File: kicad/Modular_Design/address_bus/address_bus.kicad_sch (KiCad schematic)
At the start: 21 parts

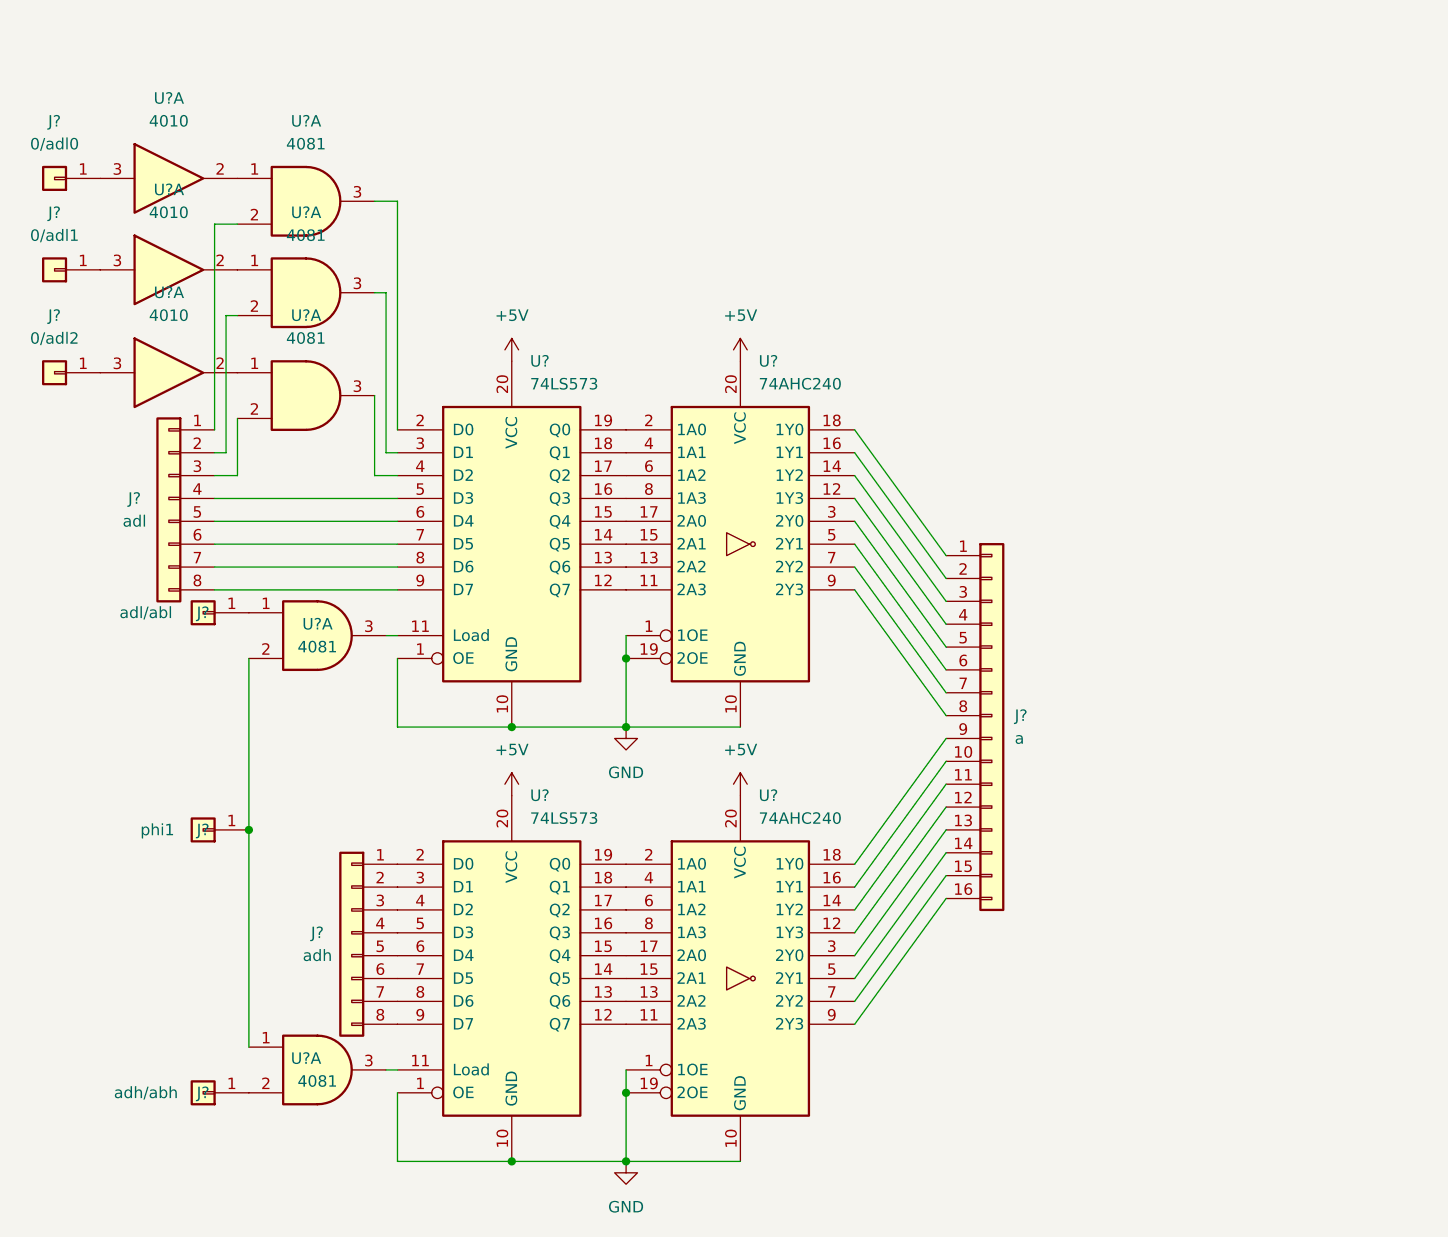
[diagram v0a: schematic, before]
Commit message: update to use regled
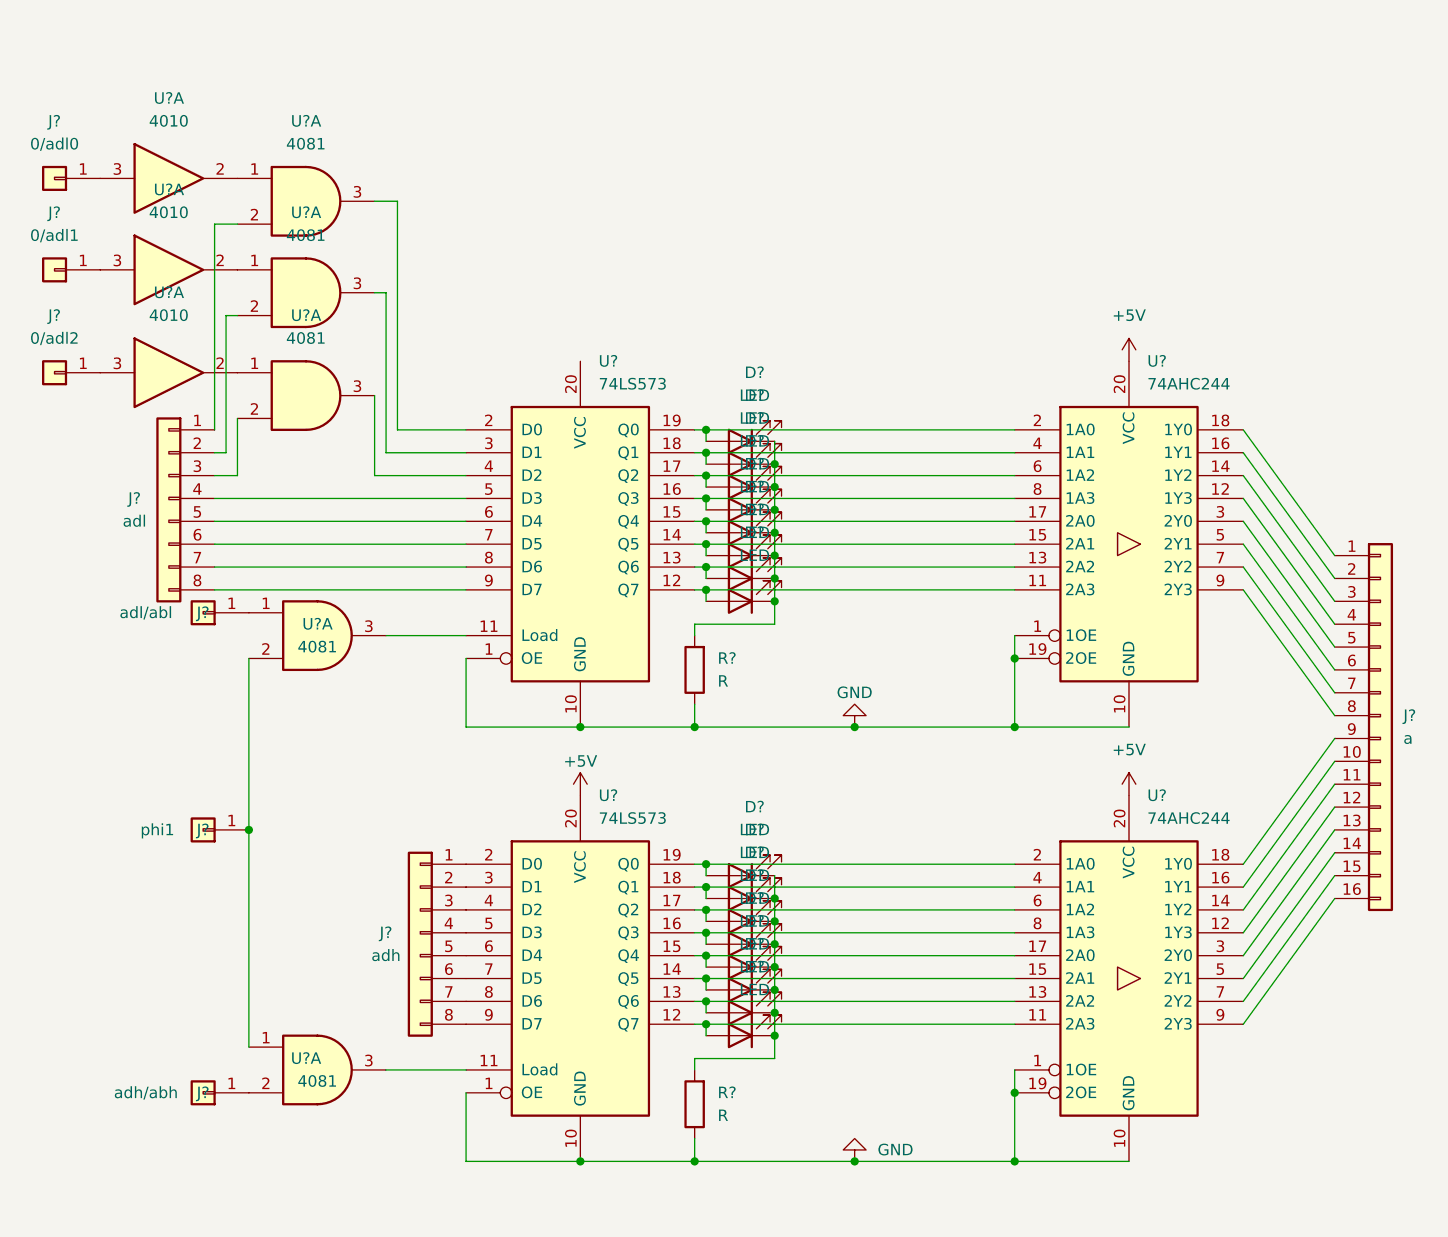
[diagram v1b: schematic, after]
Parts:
- removed U? (x2): 74AHC240, symbol 74xx:74AHC240
- removed U? (x2): 74LS573, symbol 74xx:74LS573
- added D? (x16): LED, symbol Device:LED
- added R? (x2): R, symbol Device:R
- added U? (x2): 74AHC244, symbol 74xx:74AHC244
- added U? (x2): 74LS573, symbol 74xx:74LS573
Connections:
- net +5V: now also U?.20 (VCC), U?.20 (VCC), U?.20 (VCC)
- net GND: now also R?.1, R?.1, U?.1 (1OE), U?.1 (1OE), U?.1 (OE), U?.1 (OE), U?.10 (GND), U?.10 (GND), U?.10 (GND), U?.10 (GND), U?.19 (2OE), U?.19 (2OE)
- net at J?.4 (Pin_4): now also U?.12 (1Y3)
- net at J?.3 (Pin_3): now also U?.14 (1Y2)
- net at J?.2 (Pin_2): now also U?.16 (1Y1)
- net at J?.1 (Pin_1): now also U?.18 (1Y0)
- net at J?.5 (Pin_5): now also U?.3 (2Y0)
- net at J?.6 (Pin_6): now also U?.5 (2Y1)
- net at J?.7 (Pin_7): now also U?.7 (2Y2)
- net at J?.8 (Pin_8): now also U?.9 (2Y3)
- net at J?.4 (Pin_4): now also U?.5 (D3) (x2)
- net at J?.5 (Pin_5): now also U?.6 (D4) (x2)
- net at J?.6 (Pin_6): now also U?.7 (D5) (x2)
- net at J?.7 (Pin_7): now also U?.8 (D6) (x2)
- net at J?.8 (Pin_8): now also U?.9 (D7) (x2)
- net at U?.3: now also U?.3 (D1)
- net at U?.3: now also U?.11 (Load) (x2)
- net at J?.1 (Pin_1): now also U?.2 (D0)
- net at J?.2 (Pin_2): now also U?.3 (D1)
- net at J?.3 (Pin_3): now also U?.4 (D2)
- net at J?.12 (Pin_12): now also U?.12 (1Y3)
- net at J?.11 (Pin_11): now also U?.14 (1Y2)
- net at J?.10 (Pin_10): now also U?.16 (1Y1)
- net at J?.9 (Pin_9): now also U?.18 (1Y0)
- net at J?.13 (Pin_13): now also U?.3 (2Y0)
- net at J?.14 (Pin_14): now also U?.5 (2Y1)
- net at J?.15 (Pin_15): now also U?.7 (2Y2)
- net at J?.16 (Pin_16): now also U?.9 (2Y3)
- net at U?.3: now also U?.2 (D0)
- net at U?.3: now also U?.4 (D2)
- new net: D?.1 (K), D?.1 (K), D?.1 (K), D?.1 (K), D?.1 (K), D?.1 (K), D?.1 (K), D?.1 (K), R?.2 (x2)
- new net: D?.2 (A), U?.15 (Q4), U?.17 (2A0) (x2)
- new net: D?.2 (A), U?.14 (Q5), U?.15 (2A1) (x2)
- new net: D?.2 (A), U?.19 (Q0), U?.2 (1A0) (x2)
- new net: D?.2 (A), U?.18 (Q1), U?.4 (1A1) (x2)
- new net: D?.2 (A), U?.17 (Q2), U?.6 (1A2) (x2)
- new net: D?.2 (A), U?.13 (2A2), U?.13 (Q6) (x2)
- new net: D?.2 (A), U?.16 (Q3), U?.8 (1A3) (x2)
- new net: D?.2 (A), U?.11 (2A3), U?.12 (Q7) (x2)
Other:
- moved on the sheet: J?

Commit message: fix references
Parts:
- added U2: 4081, symbol 4xxx:4081
- added unit 7 of UN1
- gave numbers to parts that had none: 33
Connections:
- net +5V: now also U1.14 (VDD), latch1.20 (VCC), U2.14 (VDD), UN1.1 (VCC), UN1.16 (VDD)
- net GND: now also U1.7 (VSS), U2.7 (VSS), UN1.8 (VSS)
- net at J2.1 (Pin_1): now also UN1.5; no longer UN1.3
- net at J3.1 (Pin_1): now also UN1.7; no longer UN1.3
- net at J4.2 (Pin_2): now also U1.6; no longer U1.2
- net at J4.3 (Pin_3): now also U1.9; no longer U1.2
- net at latch1.3 (D1): now also U1.4; no longer U1.3
- net at J7.1 (Pin_1): now also U2.2; no longer U1.2
- net at latch2.11 (Load): now also U2.3; no longer U1.3
- net at latch1.11 (Load): now also U1.11; no longer U1.3
- net at latch1.4 (D2): now also U1.10; no longer U1.3
- net at J5.1 (Pin_1): now also U1.12; no longer U1.1
- new net: U1.5, UN1.4
- new net: J6.1 (Pin_1), U1.13, U2.1
- new net: U1.8, UN1.6

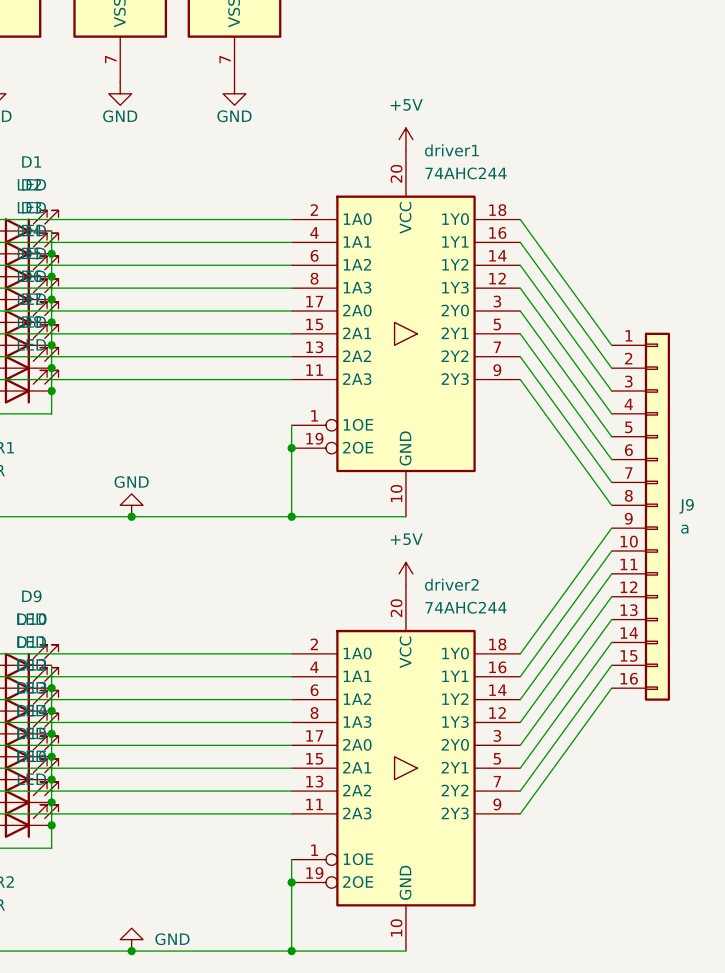
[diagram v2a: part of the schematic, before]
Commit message: fixed symbol for octal buffer
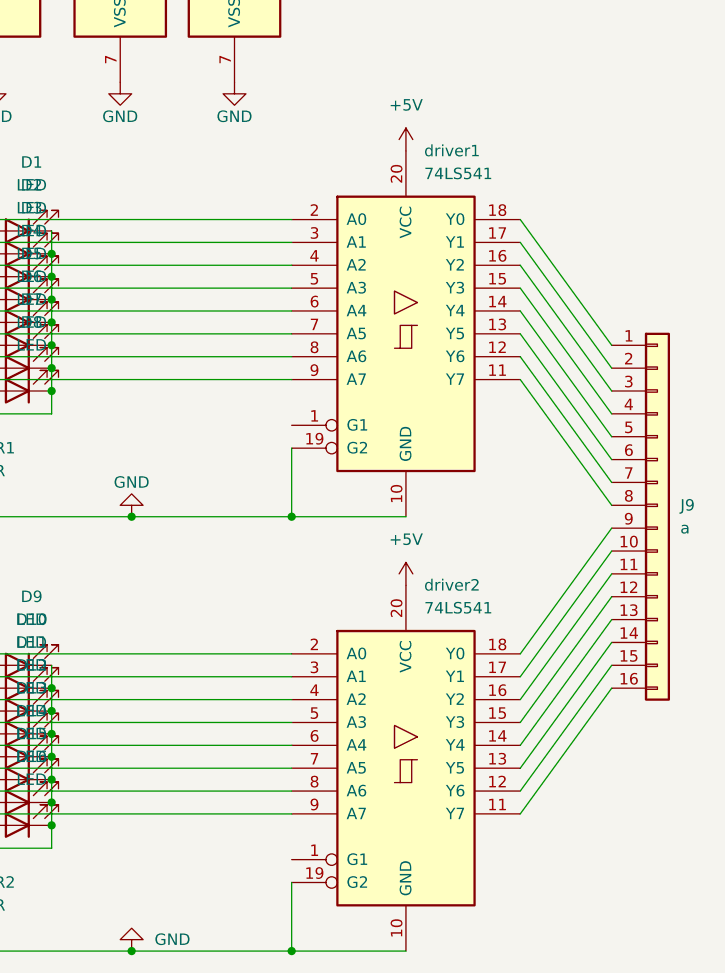
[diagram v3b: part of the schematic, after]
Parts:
- removed driver1, driver2: 74AHC244, symbol 74xx:74AHC244
- added driver1, driver2: 74LS541, symbol 74xx:74LS541
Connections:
- net +5V: now also driver1.20 (VCC), driver2.20 (VCC)
- net GND: now also driver1.10 (GND), driver1.19 (G2), driver2.10 (GND), driver2.19 (G2)
- net at D5.2 (A), latch1.15 (Q4): now also driver1.6 (A4)
- net at D14.2 (A), latch2.14 (Q5): now also driver2.7 (A5)
- net at D1.2 (A), latch1.19 (Q0): now also driver1.2 (A0)
- net at D2.2 (A), latch1.18 (Q1): now also driver1.3 (A1)
- net at D6.2 (A), latch1.14 (Q5): now also driver1.7 (A5)
- net at D13.2 (A), latch2.15 (Q4): now also driver2.6 (A4)
- net at D11.2 (A), latch2.17 (Q2): now also driver2.4 (A2)
- net at D7.2 (A), latch1.13 (Q6): now also driver1.8 (A6)
- net at D4.2 (A), latch1.16 (Q3): now also driver1.5 (A3)
- net at D15.2 (A), latch2.13 (Q6): now also driver2.8 (A6)
- net at D16.2 (A), latch2.12 (Q7): now also driver2.9 (A7)
- net at J9.12 (Pin_12): now also driver2.15 (Y3)
- net at J9.11 (Pin_11): now also driver2.16 (Y2)
- net at J9.10 (Pin_10): now also driver2.17 (Y1)
- net at J9.9 (Pin_9): now also driver2.18 (Y0)
- net at D9.2 (A), latch2.19 (Q0): now also driver2.2 (A0)
- net at J9.13 (Pin_13): now also driver2.14 (Y4)
- net at D10.2 (A), latch2.18 (Q1): now also driver2.3 (A1)
- net at J9.14 (Pin_14): now also driver2.13 (Y5)
- net at J9.15 (Pin_15): now also driver2.12 (Y6)
- net at D12.2 (A), latch2.16 (Q3): now also driver2.5 (A3)
- net at J9.16 (Pin_16): now also driver2.11 (Y7)
- net at D8.2 (A), latch1.12 (Q7): now also driver1.9 (A7)
- net at D3.2 (A), latch1.17 (Q2): now also driver1.4 (A2)
- net at J9.4 (Pin_4): now also driver1.15 (Y3)
- net at J9.3 (Pin_3): now also driver1.16 (Y2)
- net at J9.2 (Pin_2): now also driver1.17 (Y1)
- net at J9.1 (Pin_1): now also driver1.18 (Y0)
- net at J9.5 (Pin_5): now also driver1.14 (Y4)
- net at J9.6 (Pin_6): now also driver1.13 (Y5)
- net at J9.7 (Pin_7): now also driver1.12 (Y6)
- net at J9.8 (Pin_8): now also driver1.11 (Y7)
